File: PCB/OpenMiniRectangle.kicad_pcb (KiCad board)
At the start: 2 copper layers, 245.6 x 150 mm, 95 parts, among them J1 USB C Connector, J2 JTAG_TC2030, J3 Conn_01x06, J4 Conn_01x06, SW1 Boot, SW10 MX_SW_HS, SW11 MX_SW_solder, SW12 MX_SW_HS, SW13 MX_SW_solder, SW14 MX_SW_solder, SW15 MX_SW_HS, SW16 MX_SW_HS, SW17 MX_SW_solder, SW18 MX_SW_solder, SW19 MX_SW_HS, SW2 MX_SW_HS, SW20 MX_SW_solder, SW21 MX_SW_HS, SW22 MX_SW_solder, SW23 MX_SW_HS, SW24 MX_SW_HS, SW25 MX_SW_solder, SW26 MX_SW_solder, SW27 MX_SW_HS, SW28 MX_SW_HS, SW29 MX_SW_solder, SW3 MX_SW_solder, SW30 MX_SW_HS, SW31 MX_SW_solder, SW32 MX_SW_HS, SW33 MX_SW_solder, SW34 MX_SW_HS, SW35 MX_SW_solder, SW36 MX_SW_HS, SW37 MX_SW_solder, SW38 MX_SW_solder, SW39 MX_SW_HS, SW4 MX_SW_solder, SW40 MX_SW_solder, SW41 MX_SW_HS, SW42 SW_Push, SW43 SW_Push, SW5 MX_SW_HS, SW6 MX_SW_solder, SW7 MX_SW_HS, SW8 MX_SW_solder, SW9 MX_SW_HS, U1 XC6206, U2 USBLC6-2SC6, U3 RP2040, U4 W25Q128JVS, Y1 12MHz

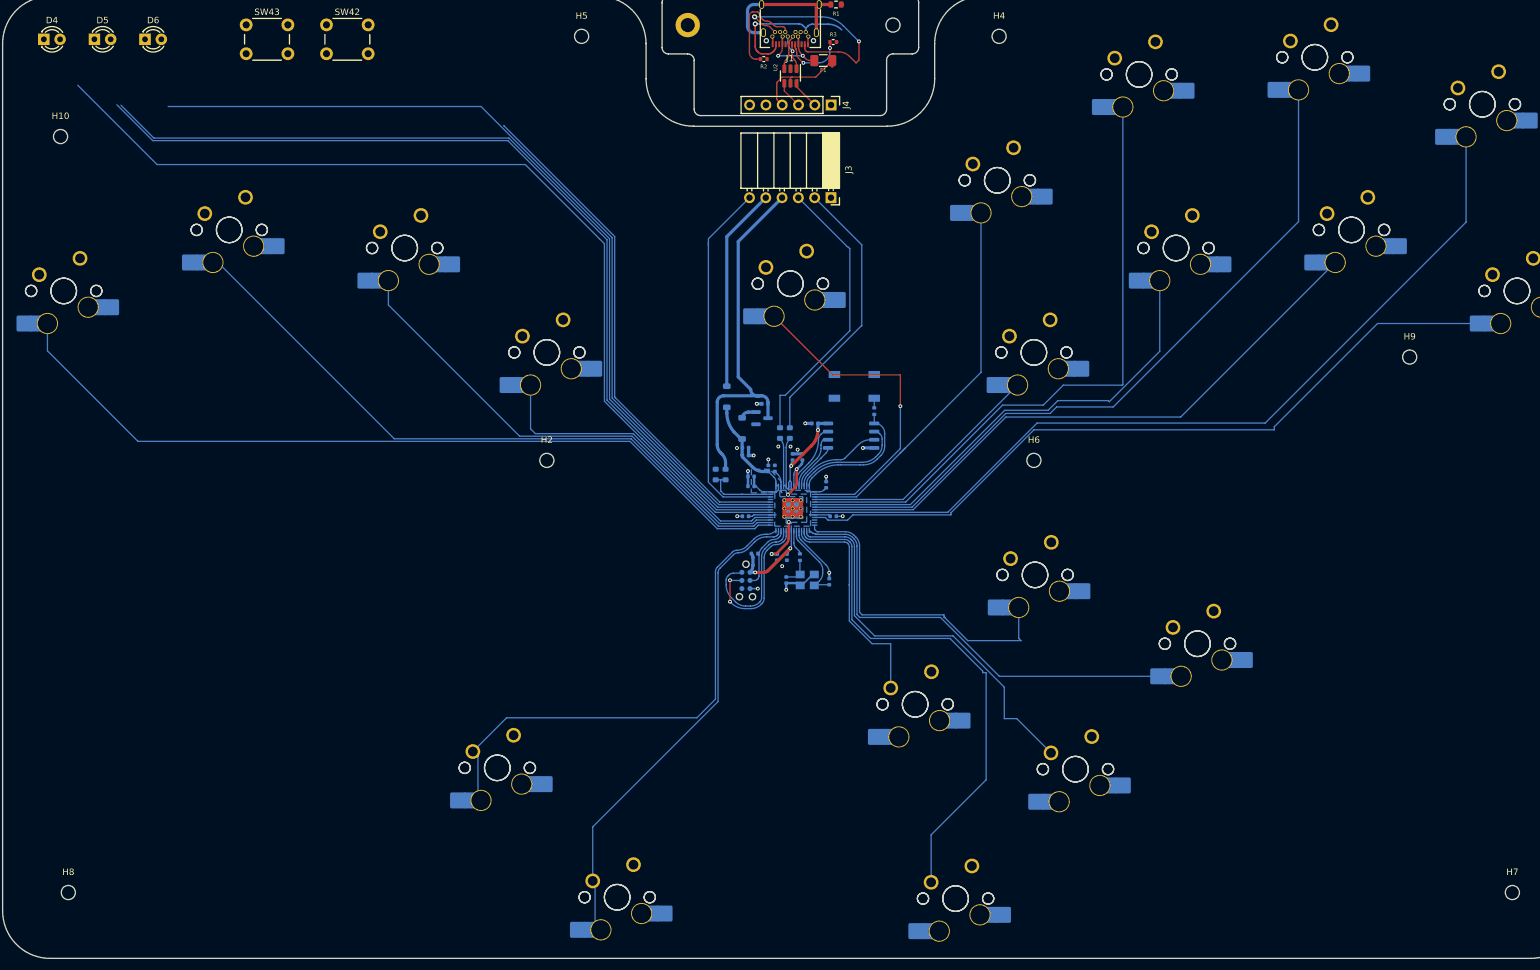
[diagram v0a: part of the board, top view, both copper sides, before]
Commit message: Added separated board for the DB
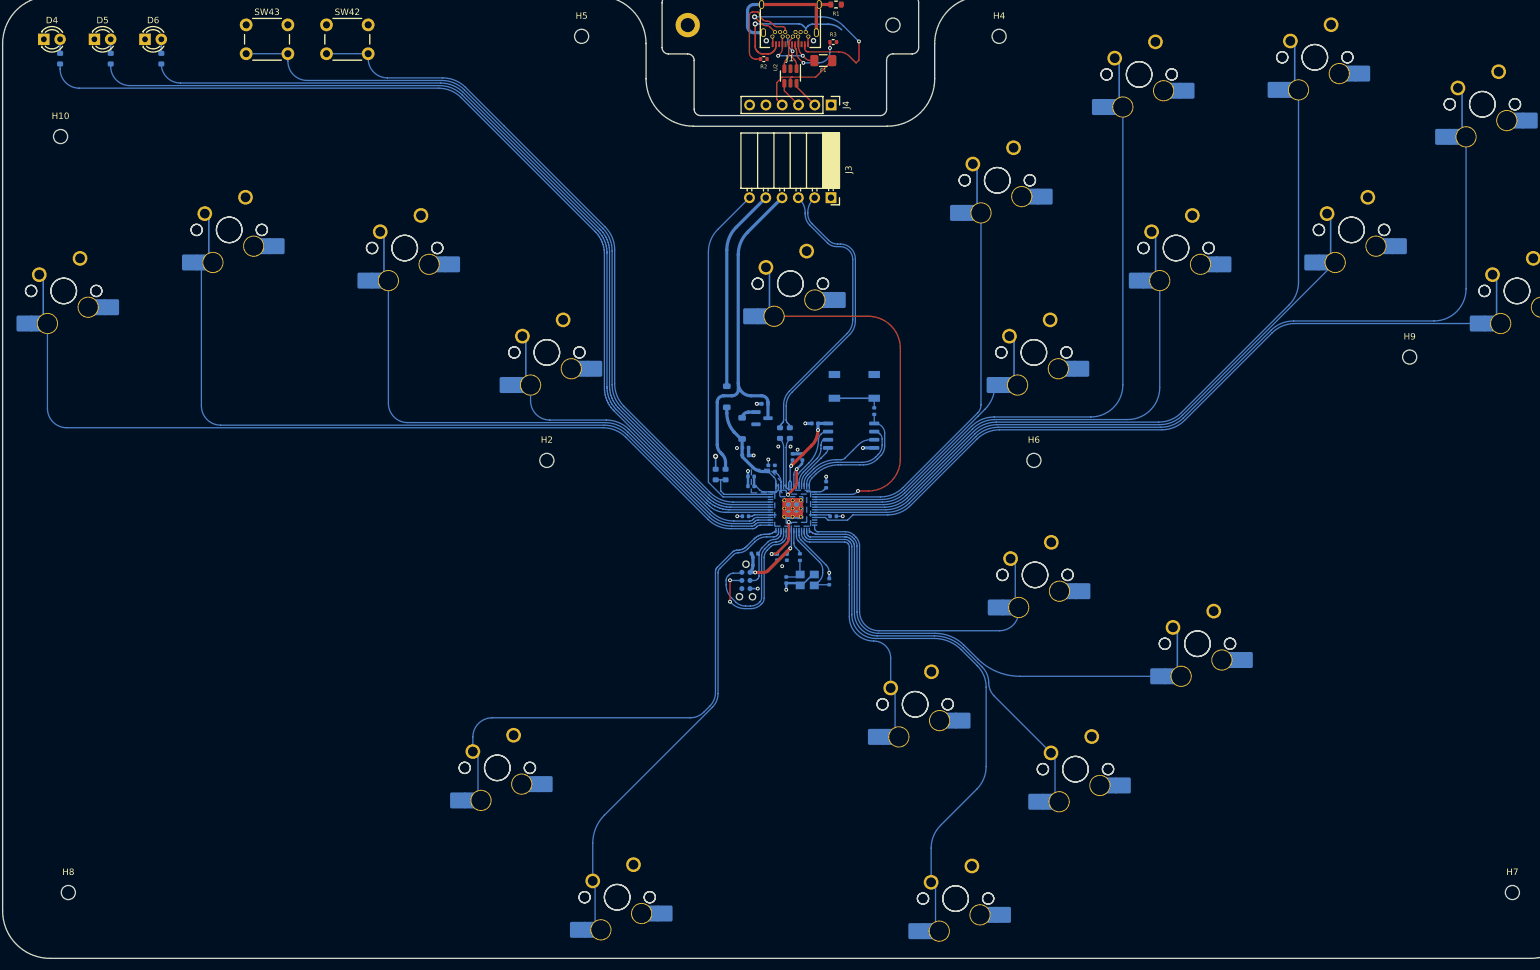
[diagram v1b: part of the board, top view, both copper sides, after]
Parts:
- added R12: 1k, Resistor_SMD:R_0603_1608Metric, B.Cu at (43.5, 33.7)
- added R13: 1k, Resistor_SMD:R_0603_1608Metric, B.Cu at (51.4, 33.7)
- added R4: 1k, Resistor_SMD:R_0603_1608Metric, B.Cu at (35.7, 33.7)
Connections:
- D4 pad 1: unconnected-(D4-K-Pad1) -> GND
- D4 pad 2: unconnected-(D4-A-Pad2) -> Net-(D4-A)
- D5 pad 1: unconnected-(D5-K-Pad1) -> GND
- D5 pad 2: unconnected-(D5-A-Pad2) -> Net-(D5-A)
- D6 pad 1: unconnected-(D6-K-Pad1) -> GND
- D6 pad 2: unconnected-(D6-A-Pad2) -> Net-(D6-A)
- SW42 pad 1: unconnected-(SW42-Pad1) -> GND
- SW42 pad 2: unconnected-(SW42-Pad2) -> HOME
- SW43 pad 1: unconnected-(SW43-Pad1) -> GND
- SW43 pad 2: unconnected-(SW43-Pad2) -> SELECT
- U3 pad 34: unconnected-(U3-GPIO22-Pad34) -> LED3
- U3 pad 35: unconnected-(U3-GPIO23-Pad35) -> LED2
- U3 pad 36: unconnected-(U3-GPIO24-Pad36) -> LED1
- U3 pad 37: PICO_LED -> SELECT
- U3 pad 38: unconnected-(U3-GPIO26/ADC0-Pad38) -> HOME
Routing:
- net LED3: track 0.00 -> 154.3 mm
- net unconnected-(U3-GPIO22-Pad34): track 150.0 -> 0.00 mm
- net LED2: track 0.00 -> 146.0 mm
- net unconnected-(U3-GPIO23-Pad35): track 142.7 -> 0.00 mm
- net unconnected-(U3-GPIO24-Pad36): track 141.9 -> 0.00 mm
- net LED1: track 0.00 -> 137.7 mm
- net PICO_LED: track 134.3 -> 0.00 mm
- net SELECT: track 0.00 -> 125.6 mm
- net HOME: track 0.00 -> 112.7 mm
- net unconnected-(U3-GPIO26/ADC0-Pad38): track 80.6 -> 0.00 mm
- net LEFT: track 106.0 -> 127.3 mm
- net DOWN: track 77.7 -> 94.7 mm
- net MS: track 114.4 -> 128.4 mm
- net LS: track 133.6 -> 147.5 mm
- net L: track 128.7 -> 141.9 mm
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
